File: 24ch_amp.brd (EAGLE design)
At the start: 92.5 x 73.4 mm, 153 parts, among them J1 TFM-125-02-XXX-D-WT, U1 TLE2426CD

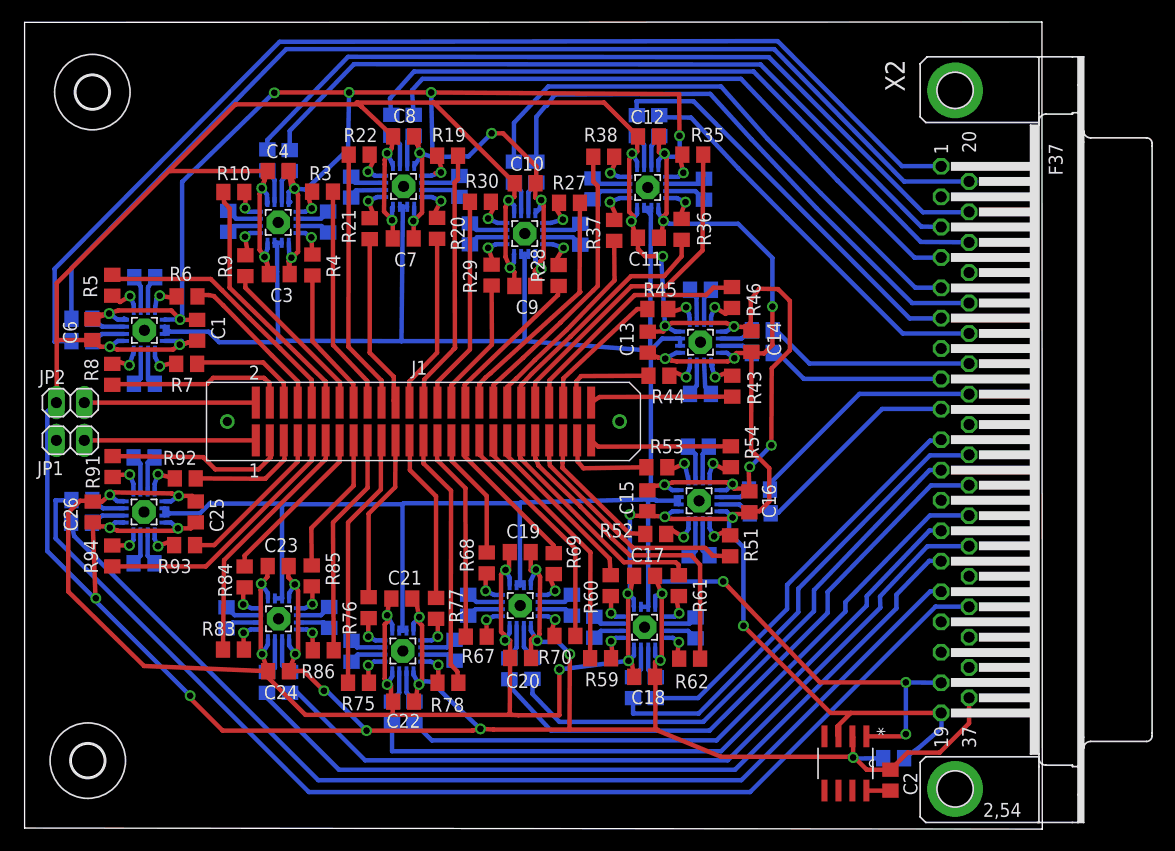
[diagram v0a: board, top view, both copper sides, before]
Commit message: minor updates to routing. Added DC-DC voltage converter/isolator to backplaneV2 & 24ch brd
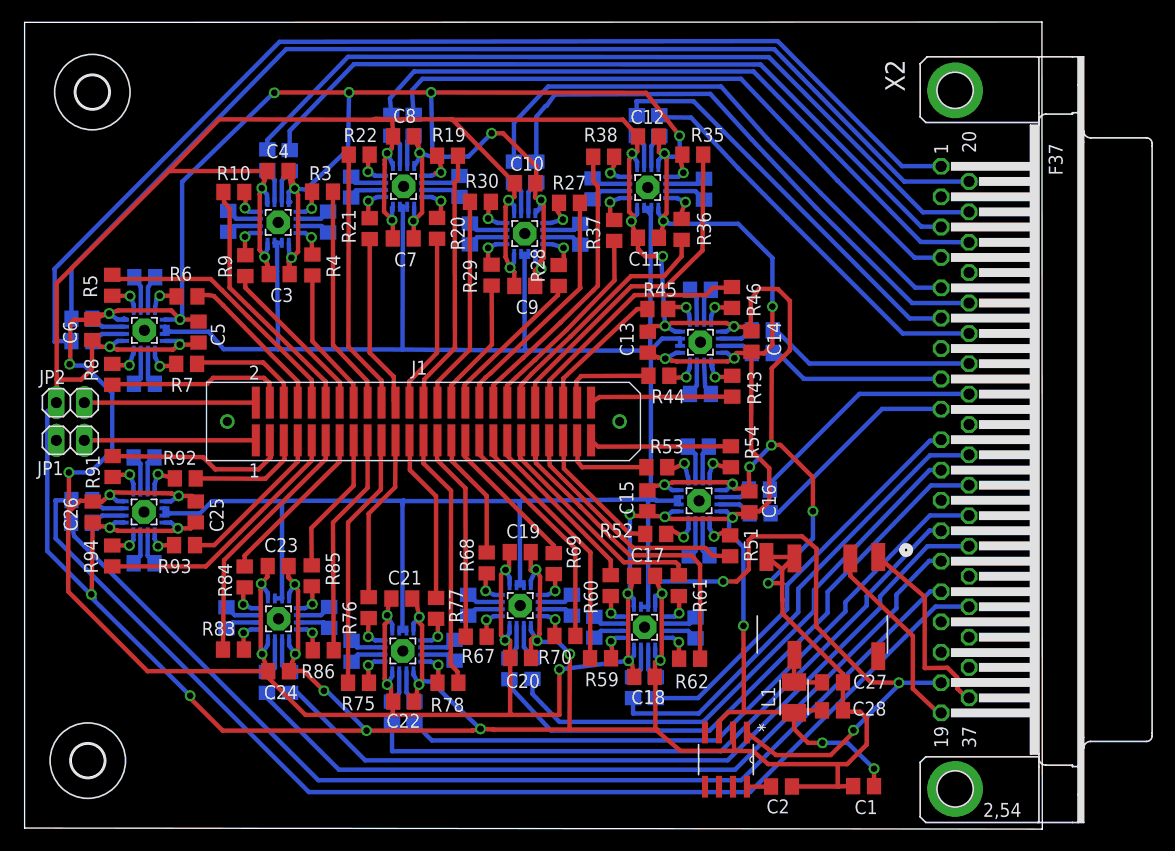
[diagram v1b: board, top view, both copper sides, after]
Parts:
- added C27, C28: 0.1uF, rcl:C0805
- added L1: (no value), resistor:L3225M
- added U$3: R1Z-1205, tuckerLib:R1Z-1205
- moved C5 74.1 mm to (15.9, 45.1), flipped to the top, turned to 270 degrees
- moved C1 73.4 mm to (76.4, 3.87), turned to 180 degrees
- moved U1 10.9 mm to (63.8, 6.29)
- moved C2 9.92 mm to (68.9, 3.84), turned to 0 degrees
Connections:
- new net +VIN: U$3.2, X2.19
- new net -VIN: U$3.1, X2.37
- new net NC2: U$3.10
- new net V+: C27.1, L1.1, U$3.7
- net GND: now also C27.2, C28.2, U$3.4, U$3.5; no longer X2.37
- net VCC: now also C28.1, L1.2; no longer X2.19
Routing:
- net GND: track 453.6 -> 485.7 mm, vias 34 -> 35
- net VCC: track 430.2 -> 454.2 mm, vias 33 -> 37
- net VREF: track 237.5 -> 259.7 mm
- net -VIN: track 0.00 -> 17.8 mm
- net +VIN: track 0.00 -> 17.7 mm
- net V+: track 0.00 -> 5.11 mm
- net IN3-: track 3.01 -> 3.61 mm
- net N$2: track 2.19 -> 2.79 mm

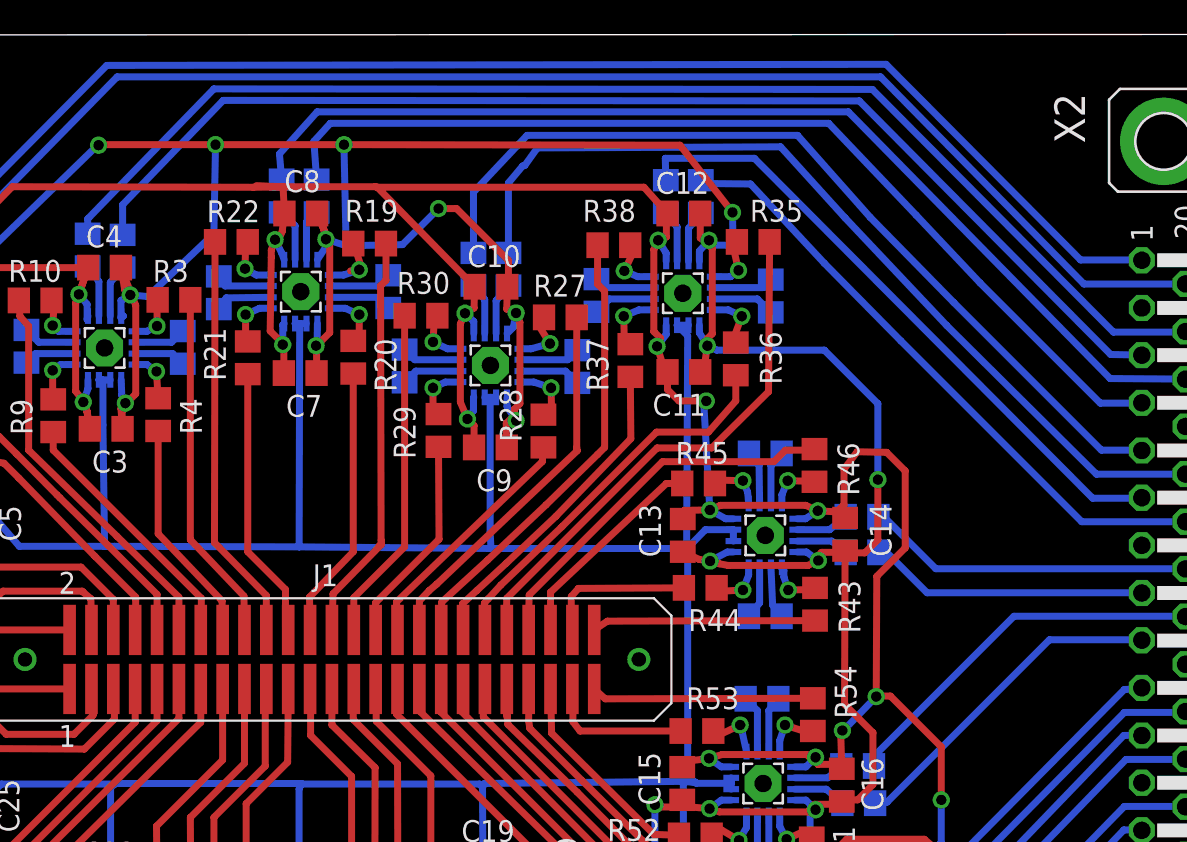
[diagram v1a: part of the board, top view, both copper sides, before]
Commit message: added new designs that use .1in pitch rather than.05, and added DC-DC isolator for VCC input to backplane
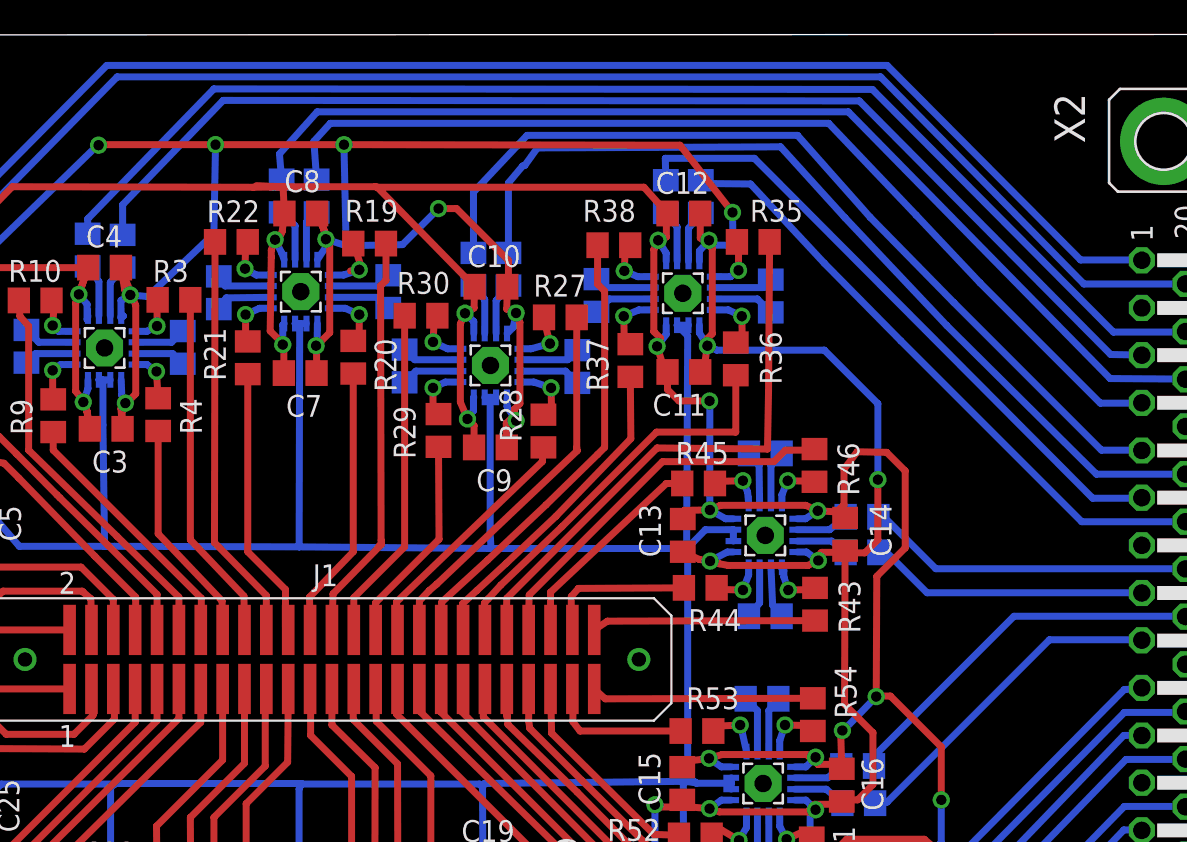
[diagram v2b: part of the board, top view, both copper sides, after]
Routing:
- net I9-: track 30.7 -> 32.7 mm
- net I9+: track 22.6 -> 23.6 mm
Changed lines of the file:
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@@
 <wire x1="59.2328" y1="45.19295" x2="58.308875" y2="45.704125" width="0.4064" layer="16"/>
 <via x="58.308875" y="45.704125" extent="1-16" drill="0.6" shape="square"/>
-<wire x1="58.308875" y1="45.704125" x2="57.959625" y2="51.895375" width="0.4064" layer="16"/>
-<wire x1="57.959625" y1="51.895375" x2="58.1025" y2="52.03825" width="0.4064" layer="16"/>
-<via x="58.1025" y="52.03825" extent="1-16" drill="0.6" shape="square"/>
-<wire x1="58.1025" y1="52.03825" x2="56.515" y2="52.03825" width="0.4064" layer="1"/>
+<wire x1="58.308875" y1="45.704125" x2="58.308875" y2="51.895375" width="0.4064" layer="16"/>
+<wire x1="58.308875" y1="51.895375" x2="58.293" y2="52.03825" width="0.4064" layer="16"/>
+<via x="58.293" y="52.03825" extent="1-16" drill="0.6" shape="square"/>
+<wire x1="58.293" y1="52.03825" x2="56.515" y2="52.03825" width="0.4064" layer="1"/>
 <wire x1="56.515" y1="52.03825" x2="55.84825" y2="52.705" width="0.4064" layer="1"/>
 <wire x1="55.84825" y1="52.705" x2="55.84825" y2="53.914" width="0.4064" layer="1"/>
@@
 <wire x1="2.82575" y1="44.2595" x2="2.82575" y2="50.89525" width="0.4064" layer="16"/>
 <wire x1="2.82575" y1="50.89525" x2="23.27275" y2="71.53275" width="0.4064" layer="16"/>
-<wire x1="23.27275" y1="71.53275" x2="68.54825" y2="71.59625" width="0.4064" layer="16"/>
-<wire x1="68.54825" y1="71.59625" x2="79.85125" y2="60.22975" width="0.4064" layer="16"/>
+<wire x1="23.27275" y1="71.53275" x2="68.61175" y2="71.53275" width="0.4064" layer="16"/>
+<wire x1="68.61175" y1="71.53275" x2="79.85125" y2="60.22975" width="0.4064" layer="16"/>
 <wire x1="79.85125" y1="60.22975" x2="83.3882" y2="60.22975" width="0.4064" layer="16"/>
 <wire x1="83.3882" y1="60.22975" x2="83.40725" y2="60.2107" width="0.4064" layer="16"/>
@@
 <contactref element="R36" pad="1"/>
 <contactref element="J1" pad="40"/>
-<wire x1="59.817" y1="53.533" x2="59.817" y2="52.03825" width="0.4064" layer="1"/>
-<wire x1="59.817" y1="52.03825" x2="58.2295" y2="50.2285" width="0.4064" layer="1"/>
-<wire x1="58.2295" y1="50.2285" x2="55.21325" y2="50.2285" width="0.4064" layer="1"/>
+<wire x1="59.817" y1="53.533" x2="59.817" y2="50.2285" width="0.4064" layer="1"/>
+<wire x1="59.817" y1="50.2285" x2="55.21325" y2="50.2285" width="0.4064" layer="1"/>
 <wire x1="55.21325" y1="50.2285" x2="49.7205" y2="44.73575" width="0.4064" layer="1"/>
 <wire x1="49.7205" y1="44.73575" x2="46.1645" y2="41.3385" width="0.4064" layer="1"/>
@@
 <contactref element="J1" pad="42"/>
 <wire x1="61.783" y1="61.2775" x2="61.7195" y2="52.5755" width="0.4064" layer="1"/>
-<wire x1="61.7195" y1="52.5755" x2="58.42" y2="49.30775" width="0.4064" layer="1"/>
-<wire x1="58.42" y1="49.30775" x2="55.245" y2="49.30775" width="0.4064" layer="1"/>
+<wire x1="61.7195" y1="52.5755" x2="61.6585" y2="49.24425" width="0.4064" layer="1"/>
+<wire x1="61.6585" y1="49.24425" x2="55.245" y2="49.30775" width="0.4064" layer="1"/>
 <wire x1="55.245" y1="49.30775" x2="46.51375" y2="40.5765" width="0.4064" layer="1"/>
 <wire x1="46.51375" y1="40.5765" x2="46.45025" y2="38.7985" width="0.4064" layer="1"/>
@@
 <wire x1="47.92345" y1="55.0672" x2="49.022" y2="55.372" width="0.4064" layer="16"/>
 <via x="49.022" y="55.372" extent="1-16" drill="0.6" shape="square"/>
-<wire x1="49.022" y1="55.372" x2="48.29175" y2="56.54425" width="0.4064" layer="1"/>
-<wire x1="48.29175" y1="56.54425" x2="48.67525" y2="56.896" width="0.4064" layer="1"/>
+<wire x1="49.022" y1="55.372" x2="48.7045" y2="56.6395" width="0.4064" layer="1"/>
+<wire x1="48.7045" y1="56.6395" x2="48.67525" y2="56.896" width="0.4064" layer="1"/>
 </signal>
 <signal name="IN8+">
@@
 <wire x1="59.5122" y1="59.2582" x2="59.97575" y2="59.6265" width="0.4064" layer="16"/>
 <via x="59.97575" y="59.6265" extent="1-16" drill="0.6" shape="square"/>
-<wire x1="59.97575" y1="59.6265" x2="59.69" y2="60.894" width="0.4064" layer="1"/>
-<wire x1="59.69" y1="60.894" x2="59.883" y2="61.2775" width="0.4064" layer="1"/>
+<wire x1="59.97575" y1="59.6265" x2="59.97575" y2="60.98925" width="0.4064" layer="1"/>
+<wire x1="59.97575" y1="60.98925" x2="59.883" y2="61.2775" width="0.4064" layer="1"/>
 </signal>
 <signal name="IN9+">
@@
 <wire x1="59.3852" y1="57.3278" x2="60.16625" y2="56.9595" width="0.4064" layer="16"/>
 <via x="60.16625" y="56.9595" extent="1-16" drill="0.6" shape="square"/>
-<wire x1="60.16625" y1="56.9595" x2="59.65825" y2="55.59175" width="0.4064" layer="1"/>
-<wire x1="59.65825" y1="55.59175" x2="59.817" y2="55.433" width="0.4064" layer="1"/>
+<wire x1="60.16625" y1="56.9595" x2="60.198" y2="55.40125" width="0.4064" layer="1"/>
+<wire x1="60.198" y1="55.40125" x2="59.817" y2="55.433" width="0.4064" layer="1"/>
 </signal>
 <signal name="IN10+">
@@
 <wire x1="54.12105" y1="59.2582" x2="53.34" y2="59.59475" width="0.4064" layer="16"/>
 <via x="53.34" y="59.59475" extent="1-16" drill="0.6" shape="square"/>
-<wire x1="53.34" y1="59.59475" x2="53.9115" y2="60.79875" width="0.4064" layer="1"/>
-<wire x1="53.9115" y1="60.79875" x2="53.68675" y2="61.087" width="0.4064" layer="1"/>
+<wire x1="53.34" y1="59.59475" x2="53.4035" y2="61.2115" width="0.4064" layer="1"/>
+<wire x1="53.4035" y1="61.2115" x2="53.68675" y2="61.087" width="0.4064" layer="1"/>
 </signal>
 <signal name="OUT9">
@@
 <wire x1="60.5663" y1="41.92905" x2="60.22975" y2="41.05275" width="0.4064" layer="16"/>
 <via x="60.22975" y="41.05275" extent="1-16" drill="0.6" shape="square"/>
-<wire x1="60.22975" y1="41.05275" x2="59.0525" y2="40.98925" width="0.4064" layer="1"/>
-<wire x1="59.0525" y1="40.98925" x2="58.70325" y2="41.17975" width="0.4064" layer="1"/>
+<wire x1="60.22975" y1="41.05275" x2="59.0525" y2="41.0845" width="0.4064" layer="1"/>
+<wire x1="59.0525" y1="41.0845" x2="58.70325" y2="41.17975" width="0.4064" layer="1"/>
 </signal>
 <signal name="IN12+">
@@
 <wire x1="60.5028" y1="46.7487" x2="60.22975" y2="47.40275" width="0.4064" layer="16"/>
 <via x="60.22975" y="47.40275" extent="1-16" drill="0.6" shape="square"/>
-<wire x1="60.22975" y1="47.40275" x2="59.02075" y2="47.4345" width="0.4064" layer="1"/>
-<wire x1="59.02075" y1="47.4345" x2="58.608" y2="47.244" width="0.4064" layer="1"/>
+<wire x1="60.22975" y1="47.40275" x2="58.989" y2="47.371" width="0.4064" layer="1"/>
+<wire x1="58.989" y1="47.371" x2="58.608" y2="47.244" width="0.4064" layer="1"/>
 </signal>
 <signal name="IN12-">
@@
 <wire x1="60.1853" y1="32.81045" x2="60.071" y2="33.2105" width="0.4064" layer="16"/>
 <via x="60.071" y="33.2105" extent="1-16" drill="0.6" shape="square"/>
-<wire x1="60.071" y1="33.2105" x2="58.7985" y2="32.60725" width="0.4064" layer="1"/>
-<wire x1="58.7985" y1="32.60725" x2="58.51275" y2="32.86125" width="0.4064" layer="1"/>
+<wire x1="60.071" y1="33.2105" x2="58.735" y2="33.147" width="0.4064" layer="1"/>
+<wire x1="58.735" y1="33.147" x2="58.51275" y2="32.86125" width="0.4064" layer="1"/>
 </signal>
 <signal name="IN24-">
@@
 <wire x1="62.3697" y1="32.30245" x2="62.6745" y2="33.2105" width="0.4064" layer="16"/>
 <via x="62.6745" y="33.2105" extent="1-16" drill="0.6" shape="square"/>
-<wire x1="62.6745" y1="33.2105" x2="63.942" y2="32.79775" width="0.4064" layer="1"/>
-<wire x1="63.942" y1="32.79775" x2="64.29375" y2="32.86375" width="0.4064" layer="1"/>
+<wire x1="62.6745" y1="33.2105" x2="63.97375" y2="33.17875" width="0.4064" layer="1"/>
+<wire x1="63.97375" y1="33.17875" x2="64.29375" y2="32.86375" width="0.4064" layer="1"/>
 </signal>
 <signal name="OUT23">
